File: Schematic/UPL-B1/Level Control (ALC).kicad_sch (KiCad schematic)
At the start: 102 parts, among them P53 TestPoint, P54 TestPoint, P55 TestPoint, P56 TestPoint, P57 TestPoint, P58 TestPoint, X50 Conn_01x03_Pin_Bridge, X51 Conn_01x03_Pin_Bridge, X52 Conn_01x03_Pin_Bridge

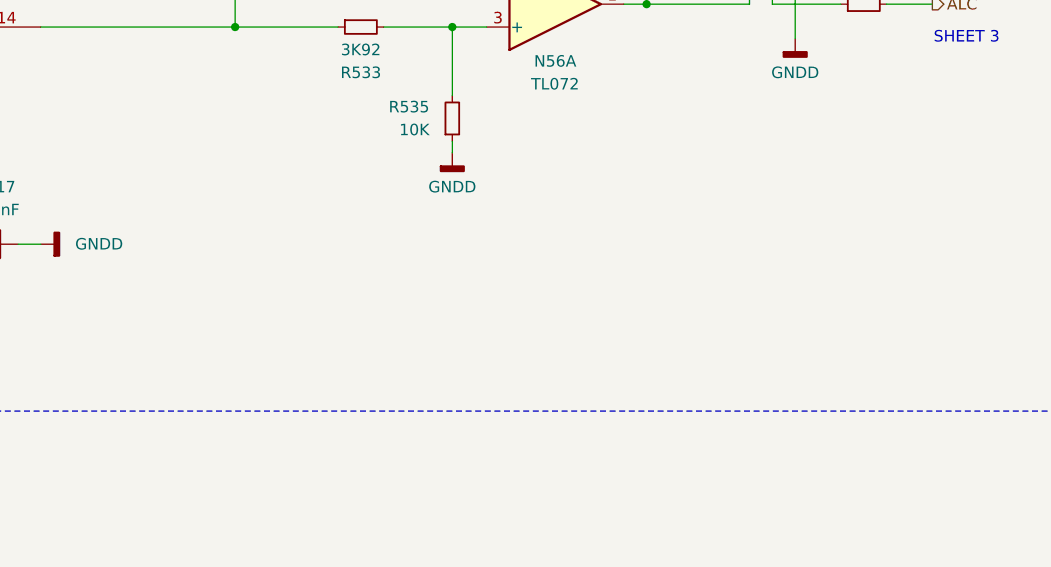
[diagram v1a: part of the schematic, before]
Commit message: Annotate with reverse engineering clues
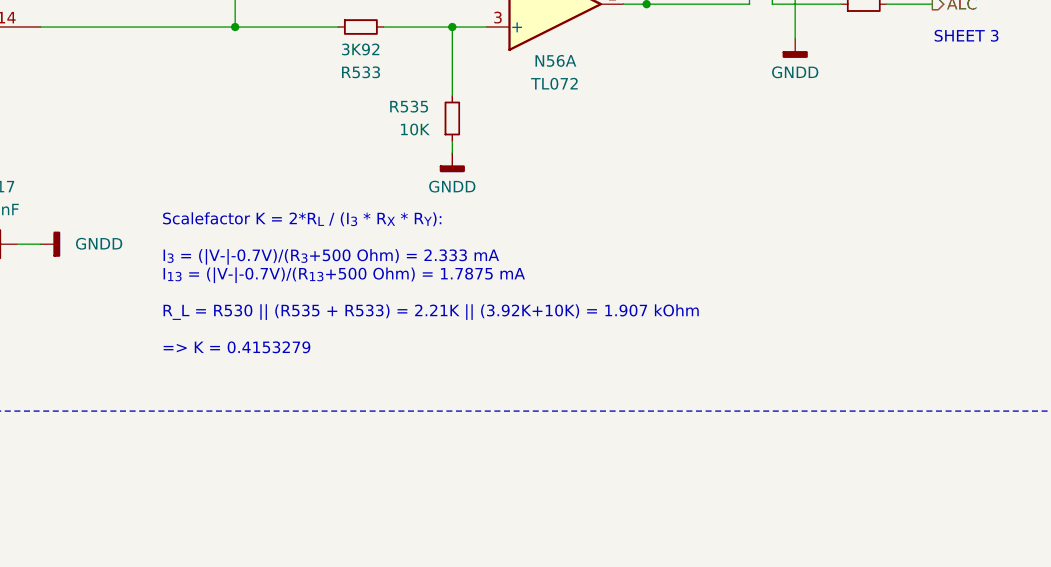
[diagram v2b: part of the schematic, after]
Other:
- note added: "Scalefactor K = 2*R_{L} / (I_{3} * R_{X} * R_{Y}): I_{3} = (|V-|-0.7V)/(R_{3}+500 Ohm) = 2.333 mA I_{13} = (|V-|-0.7V)/(R_{13}+500 Ohm) = 1.7875 mA R_L = R530 || (R535 + R533) = 2.21K || (3.92K+10K) = 1.907 kOhm => K = 0.4153279"
